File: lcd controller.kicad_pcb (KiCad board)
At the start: 2 copper layers, 80 x 36 mm, 13 parts, among them J1 DATA, J2 DISPLAY, Q1 BC817W, U1 ATmega328PB-AU

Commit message: Shrink board
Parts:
- removed H3, H4: MountingHole, MountingHole:MountingHole_2.5mm_Pad
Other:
- board size 80 x 36 mm -> 49.3 x 36 mm
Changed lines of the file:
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@@
     (tracks 178)
     (zones 0)
-    (modules 13)
+    (modules 11)
     (nets 26)
   )
@@
     (add_net /SS)
     (add_net GND)
+    (add_net "Net-(J1-Pad4)")
     (add_net "Net-(J2-Pad16)")
     (add_net "Net-(Q1-Pad1)")
     (add_net "Net-(R1-Pad2)")
+    (add_net "Net-(U1-Pad12)")
+    (add_net "Net-(U1-Pad19)")
+    (add_net "Net-(U1-Pad20)")
+    (add_net "Net-(U1-Pad22)")
+    (add_net "Net-(U1-Pad23)")
+    (add_net "Net-(U1-Pad24)")
+    (add_net "Net-(U1-Pad25)")
+    (add_net "Net-(U1-Pad3)")
   )
   (net_class VCC ""
@@
     (pad 1 thru_hole circle (at 0 0) (size 5 5) (drill 2.5) (layers *.Cu *.Mask))
   )
-  (module MountingHole:MountingHole_2.5mm_Pad locked (layer F.Cu)
-    (at 187.5 62.5)
-    (descr "Mounting Hole 2.5mm")
-    (tags "mounting hole 2.5mm")
-    (attr virtual)
-    (fp_text reference H3 (at 0 -3.5) (layer F.SilkS) hide
-      (effects (font (size 1 1) (thickness 0.15)))
-    )
-    (fp_text value MountingHole (at 0 3.5) (layer F.Fab) hide
-      (effects (font (size 1 1) (thickness 0.15)))
-    )
-    (fp_text user %R (at 0.3 0) (layer F.Fab) hide
-      (effects (font (size 1 1) (thickness 0.15)))
-    )
-    (fp_circle (center 0 0) (end 2.5 0) (layer Cmts.User) (width 0.15))
-    (fp_circle (center 0 0) (end 2.75 0) (layer F.CrtYd) (width 0.05))
-    (pad 1 thru_hole circle (at 0 0) (size 5 5) (drill 2.5) (layers *.Cu *.Mask))
-  )
-  (module MountingHole:MountingHole_2.5mm_Pad locked (layer F.Cu)
-    (at 187.5 93.5)
-    (descr "Mounting Hole 2.5mm")
-    (tags "mounting hole 2.5mm")
-    (attr virtual)
-    (fp_text reference H4 (at 0 -3.5) (layer F.SilkS) hide
-      (effects (font (size 1 1) (thickness 0.15)))
-    )
-    (fp_text value MountingHole (at 0 3.5) (layer F.Fab) hide
-      (effects (font (size 1 1) (thickness 0.15)))
-    )
-    (fp_text user %R (at 0.3 0) (layer F.Fab) hide
-      (effects (font (size 1 1) (thickness 0.15)))
-    )
-    (fp_circle (center 0 0) (end 2.5 0) (layer Cmts.User) (width 0.15))
-    (fp_circle (center 0 0) (end 2.75 0) (layer F.CrtYd) (width 0.05))
-    (pad 1 thru_hole circle (at 0 0) (size 5 5) (drill 2.5) (layers *.Cu *.Mask))
-  )
   (gr_line (start 110 96) (end 110 60) (layer Edge.Cuts) (width 0.2))
-  (gr_line (start 190 96) (end 110 96) (layer Edge.Cuts) (width 0.2))
-  (gr_line (start 190 60) (end 190 96) (layer Edge.Cuts) (width 0.2))
-  (gr_line (start 110 60) (end 190 60) (layer Edge.Cuts) (width 0.2))
+  (gr_line (start 159.3 96) (end 110 96) (layer Edge.Cuts) (width 0.2))
+  (gr_line (start 159.3 60) (end 159.3 96) (layer Edge.Cuts) (width 0.2))
+  (gr_line (start 110 60) (end 159.3 60) (layer Edge.Cuts) (width 0.2))
   (segment (start 127.1 80.125) (end 127.275 80.3) (width 0.5) (layer F.Cu) (net 1) (status 30))
   (segment (start 127.1 77.85) (end 127.1 80.125) (width 0.4) (layer F.Cu) (net 1) (status 30))

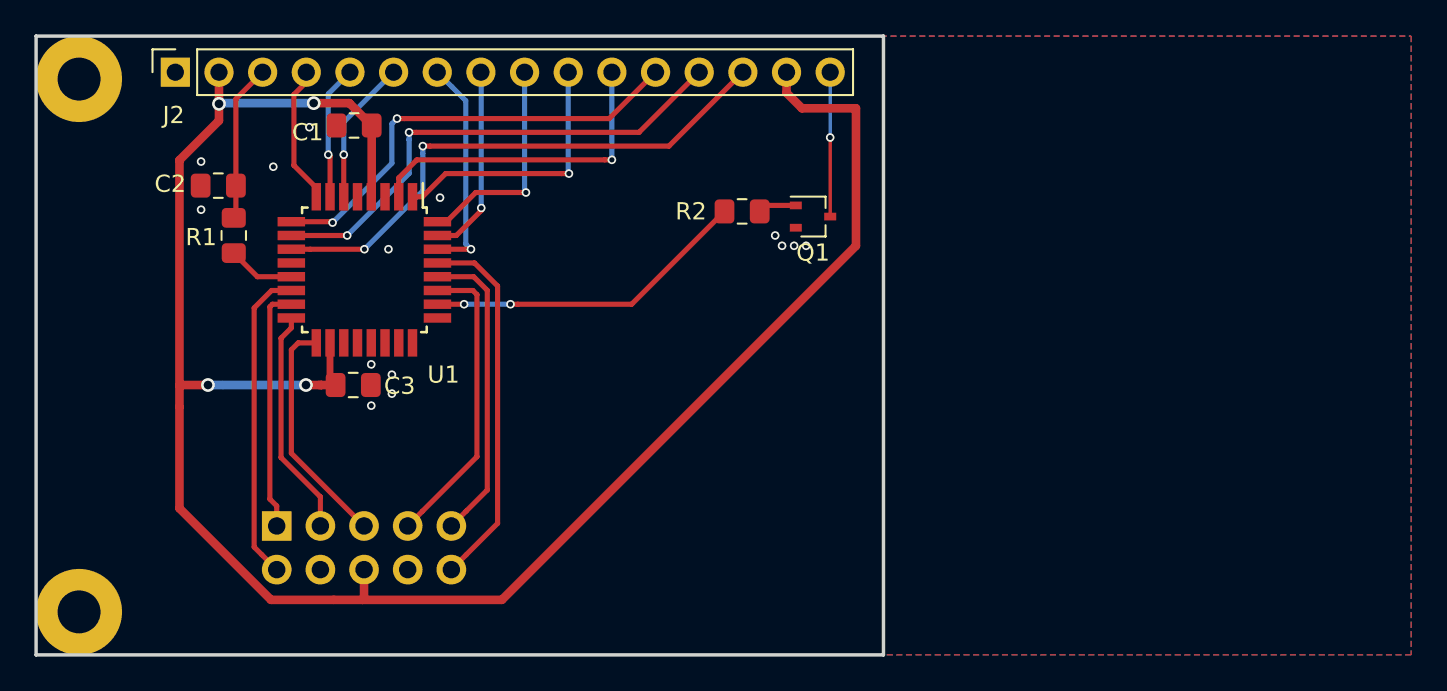
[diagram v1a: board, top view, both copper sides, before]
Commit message: Shrunk board
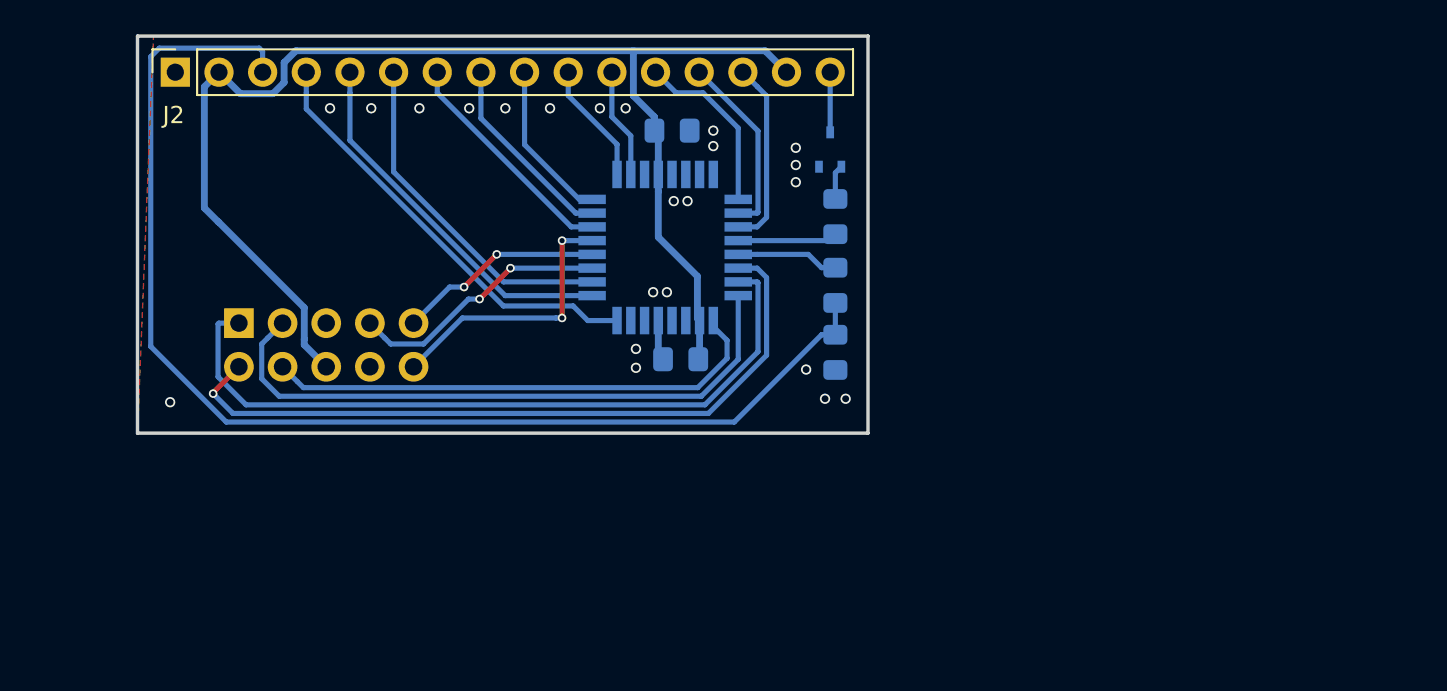
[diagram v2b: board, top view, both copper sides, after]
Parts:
- removed H1, H2: MountingHole, MountingHole:MountingHole_2.5mm_Pad
- C1, C2, C3, Q1, R1, R2, U1: moved to B.Cu
- moved C2 37.2 mm to (156.5, 78.4), turned to 90 degrees
- moved R1 35.1 mm to (156.5, 74.5), turned to 90 degrees
- moved C3 19.1 mm to (147.5, 78.8), turned to 180 degrees
- moved C1 18.5 mm to (147.0, 65.5), turned to 0 degrees
- moved U1 17.5 mm to (146.6, 72.3)
- moved J1 12.0 mm to (121.8, 76.7)
- moved R2 5.43 mm to (156.5, 70.5), turned to 270 degrees
- moved Q1 4.03 mm to (156.2, 66.6), turned to 90 degrees
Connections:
- J1 pad 4: (no net) -> /SCK
- J1 pad 5: /SCK -> GND
- U1 pad 12: (no net) -> /BACKLIGHT
- U1 pad 24: (no net) -> /RS
- U1 pad 25: (no net) -> /RW
- U1 pad 26: /BACKLIGHT -> /E
- U1 pad 6: /E -> (no net)
- U1 pad 7: /RW -> (no net)
- U1 pad 8: /RS -> (no net)
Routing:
- net /CON: track 9.17 -> 70.5 mm
- net VCC: track 116.9 -> 75.7 mm, vias 4 -> 0
- net /MOSI: track 14.2 -> 42.9 mm
- net /SS: track 18.4 -> 42.7 mm, vias 0 -> 1
- net /MISO: track 13.3 -> 36.5 mm
- net /D7: track 32.1 -> 10.9 mm, vias 2 -> 0
- net /D6: track 29.1 -> 10.7 mm, vias 2 -> 0
- net /RS: track 8.09 -> 25.3 mm
- net /SCK: track 13.6 -> 29.6 mm
- net /D5: track 26.2 -> 10.3 mm, vias 2 -> 0
- net /RW: track 7.81 -> 21.8 mm, vias 1 -> 0
- net /BACKLIGHT: track 18.9 -> 5.81 mm, vias 2 -> 0
- net /D4: track 19.0 -> 6.41 mm, vias 1 -> 0
- net /E: track 8.45 -> 20.0 mm, vias 1 -> 0
- net /D3: track 15.6 -> 7.13 mm, vias 1 -> 0
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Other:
- board size 49.3 x 36 mm -> 42.5 x 23.1 mm
- net class Default: trace_width 0.2 -> 0.3
- net class GND added: clearance 0.2, trace_width 0.4, via_dia 0.6, via_drill 0.4
- net class VCC: trace_width 0.5 -> 0.4; via_dia 0.8 -> 0.6; via_drill 0.5 -> 0.4

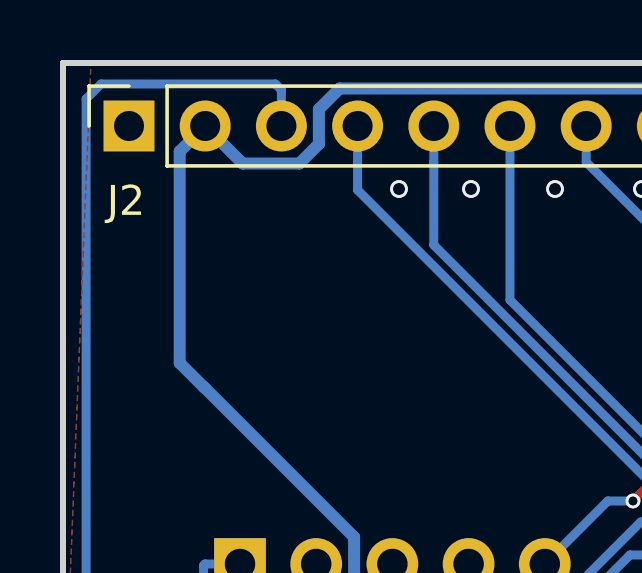
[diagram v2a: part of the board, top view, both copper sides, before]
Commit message: Drag VCC line
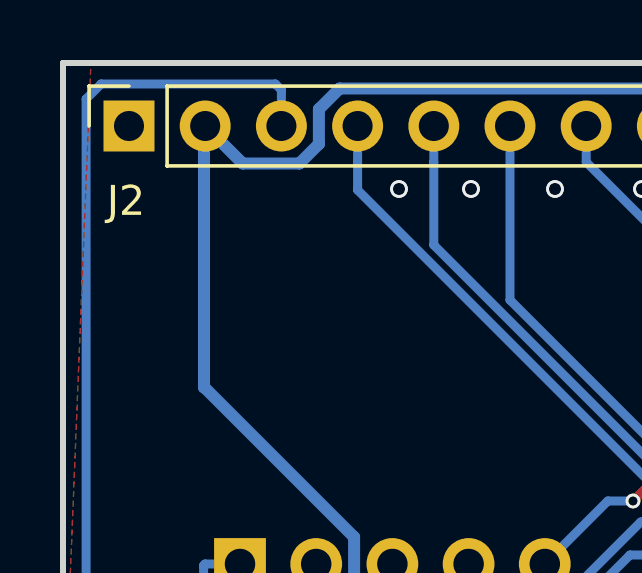
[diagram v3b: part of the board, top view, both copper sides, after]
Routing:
- net VCC: track 75.7 -> 75.1 mm
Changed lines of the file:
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@@
   (segment (start 145.975 64.7) (end 144.750001 63.475001) (width 0.4) (layer B.Cu) (net 1))
   (segment (start 145.975 65.5) (end 145.975 64.7) (width 0.4) (layer B.Cu) (net 1))
-  (segment (start 119.790001 62.949999) (end 120.64 62.1) (width 0.4) (layer B.Cu) (net 1))
-  (segment (start 120.6064 70.816399) (end 119.790001 70) (width 0.4) (layer B.Cu) (net 1))
-  (segment (start 120.616399 70.816399) (end 120.6064 70.816399) (width 0.4) (layer B.Cu) (net 1))
-  (segment (start 125.603601 75.803601) (end 120.616399 70.816399) (width 0.4) (layer B.Cu) (net 1))
-  (segment (start 125.6 77.96) (end 125.6 77.635065) (width 0.4) (layer B.Cu) (net 1))
-  (segment (start 125.603601 77.631464) (end 125.603601 75.803601) (width 0.4) (layer B.Cu) (net 1))
-  (segment (start 125.6 77.635065) (end 125.603601 77.631464) (width 0.4) (layer B.Cu) (net 1))
-  (segment (start 119.790001 70) (end 119.790001 62.949999) (width 0.4) (layer B.Cu) (net 1))
-  (segment (start 126.88 79.24) (end 125.6 77.96) (width 0.4) (layer B.Cu) (net 1))
   (segment (start 146.2 69.045002) (end 146.2 68.05) (width 0.4) (layer B.Cu) (net 1))
   (segment (start 148.475001 73.975001) (end 146.2 71.7) (width 0.4) (layer B.Cu) (net 1))
@@
   (segment (start 123.780001 63.350001) (end 124.430001 62.700001) (width 0.4) (layer B.Cu) (net 1))
   (segment (start 120.64 62.1) (end 121.890001 63.350001) (width 0.4) (layer B.Cu) (net 1))
+  (segment (start 120.6 62.14) (end 120.64 62.1) (width 0.4) (layer B.Cu) (net 1))
+  (segment (start 120.6 70.809999) (end 120.6 62.14) (width 0.4) (layer B.Cu) (net 1))
+  (segment (start 125.603601 75.803601) (end 120.616399 70.816399) (width 0.4) (layer B.Cu) (net 1))
+  (segment (start 125.6 77.635065) (end 125.603601 77.631464) (width 0.4) (layer B.Cu) (net 1))
+  (segment (start 120.6064 70.816399) (end 120.6 70.809999) (width 0.4) (layer B.Cu) (net 1))
+  (segment (start 125.6 77.96) (end 125.6 77.635065) (width 0.4) (layer B.Cu) (net 1))
+  (segment (start 120.616399 70.816399) (end 120.6064 70.816399) (width 0.4) (layer B.Cu) (net 1))
+  (segment (start 125.603601 77.631464) (end 125.603601 75.803601) (width 0.4) (layer B.Cu) (net 1))
+  (segment (start 126.88 79.24) (end 125.6 77.96) (width 0.4) (layer B.Cu) (net 1))
   (via (at 154.2 66.5) (size 0.6) (drill 0.4) (layers F.Cu B.Cu) (net 2))
   (via (at 149.4 65.5) (size 0.6) (drill 0.4) (layers F.Cu B.Cu) (net 2))
